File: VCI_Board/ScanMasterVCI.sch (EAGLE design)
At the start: 80 parts, among them IC1 XMEGA16A4A, IC2 CD4081B, IC3 SN74AHCT1G04, IC4 SN74AHCT1G04, IC6 TL331, IC7 74AHCT1G32DBV, IC8 SN74AHCT1G04, Q1 MMBT4403, Q2 MMBT4403LT1SMD, Q3 MMBT4403, Q4 MMBT3904, Q5 MMBT3904, Q6 MMBT4403, Q7 MMBT4403, Q8 MMBT4403, Q9 MMBT4403, U1 MAX17502FATB+, U3 MAX17502EATB+, U4 MAX13444EASA+

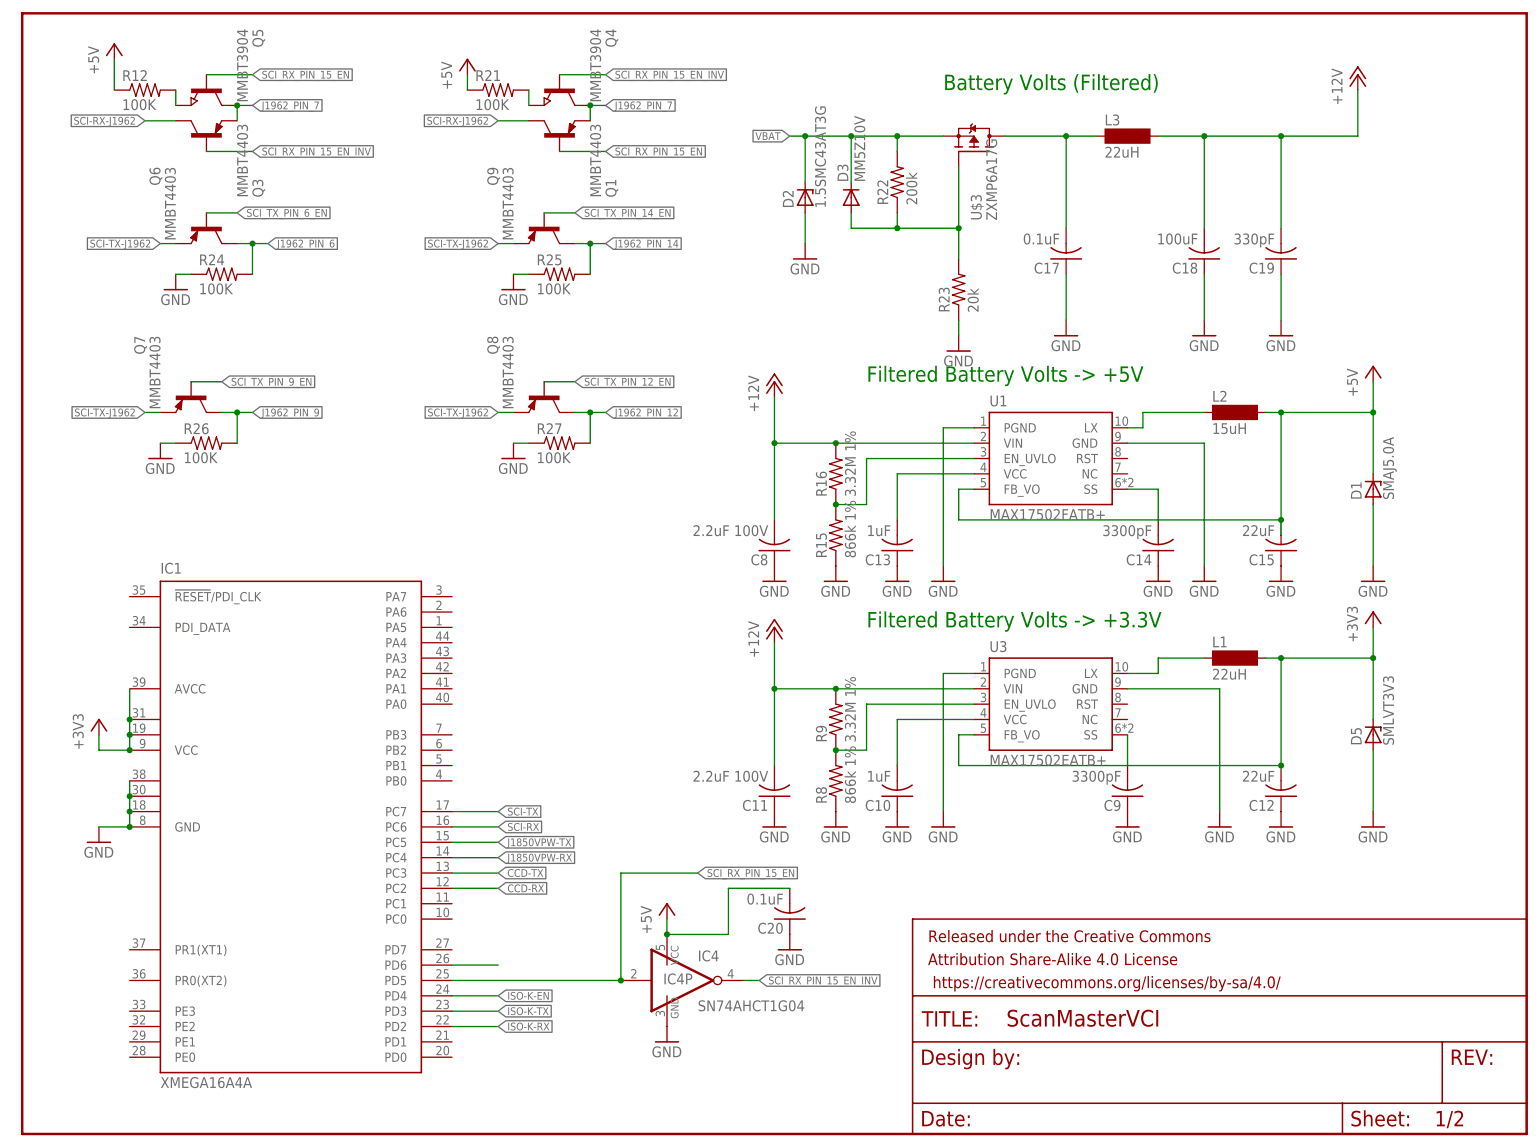
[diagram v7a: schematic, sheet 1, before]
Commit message: Added more sophisticated MUX for SCI. Moved around some pins to accomodate SPI programming. Added external headers for 4-pin RS-232, 6-pin ICSP, and 16-pin J1962.
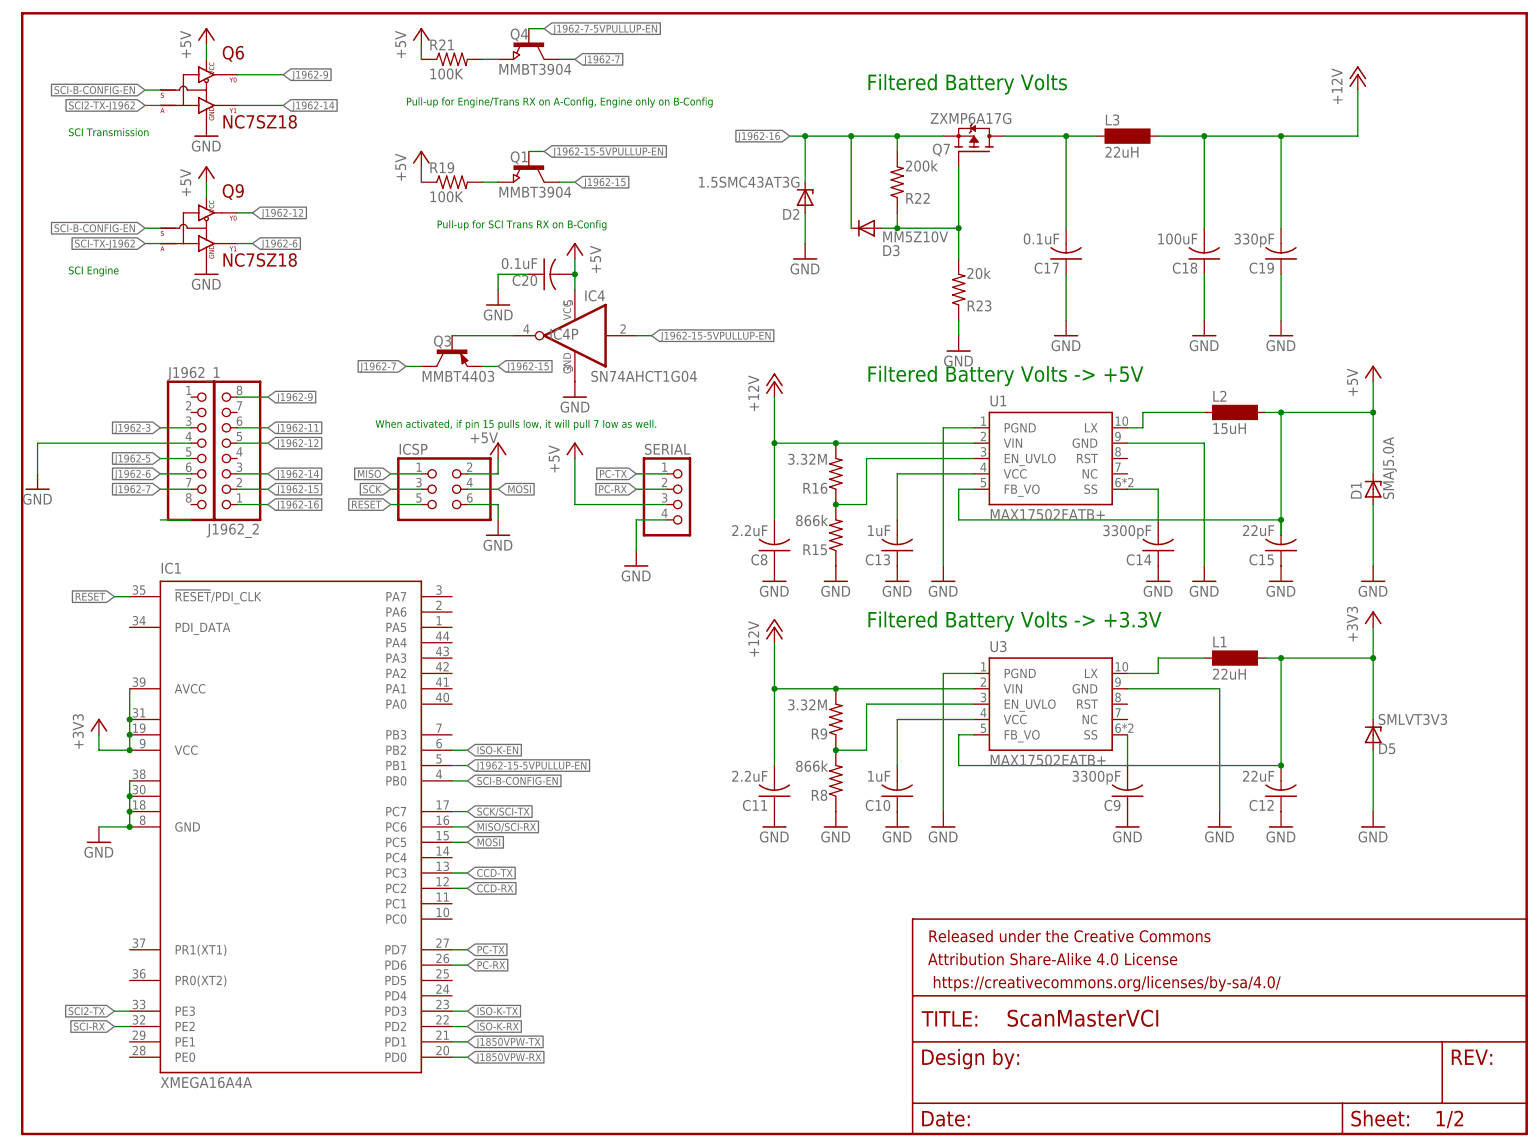
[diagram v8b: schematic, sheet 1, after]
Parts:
- removed IC3: SN74AHCT1G04, 74xx-little-us:74AHC1G04DBV
- removed Q5: MMBT3904, semicon-smd-ipc:NPN-TRANSISTOR_SOT23
- removed Q8: MMBT4403, transistor-pnp:MMBT4403LT1SMD
- removed R12, R18, R24, R25, R26, R27: 100K, adafruit:R-US_R0805W
- removed U$3: ZXMP6A17G, customics:ZXMP6A17G
- added ICSP: (no value), pinhead:PINHD-2X3
- added J1962_1, J1962_2: (no value), pinhead:PINHD-1X8
- added SERIAL: (no value), pinhead:PINHD-1X4
- C1, C16, C2, C3, C5, C6: value 0.1uF 16V -> 0.1uF
- C11, C8: value 2.2uF 100V -> 2.2uF
- C7: value 220pF 16V -> 220pF
- Q1: value MMBT4403 -> MMBT3904; device transistor-pnp:MMBT4403LT1SMD -> semicon-smd-ipc:NPN-TRANSISTOR_SOT23
- Q6, Q9: value MMBT4403 -> NC7SZ18; device transistor-pnp:MMBT4403LT1SMD -> customics:NC7SZ18
- Q7: value MMBT4403 -> ZXMP6A17G; device transistor-pnp:MMBT4403LT1SMD -> customics:ZXMP6A17G
- R15, R8: value 866k 1% -> 866k
- R16, R9: value 3.32M 1% -> 3.32M
- renumbered U$1 to D4, U$2 to U2
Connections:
- net J1962_PIN_2 renamed J1962-2
- removed net J1962_PIN_11: R1.1
- removed net J1962_PIN_12: Q8.C, R27.2
- removed net J1962_PIN_14: Q9.C, R25.2
- removed net J1962_PIN_3: R2.1
- removed net J1962_PIN_6: Q6.C, R24.2
- removed net J1962_PIN_7: C7.2, Q1.E, Q3.E, Q4.C, Q5.C, U2.LIN
- removed net J1962_PIN_9: Q7.C, R26.2
- removed net N$13: Q5.E, R12.2
- removed net N$22: IC1.PD6
- removed net SCI-RX-J1962: IC2C.I0, IC2C.I1, Q1.C, Q3.C
- removed net SCI_RX_PIN_15_EN: IC1.PD5, IC4A.I, Q1.B, Q5.B
- removed net SCI_RX_PIN_15_EN_INV: IC4A.O, Q3.B, Q4.B
- removed net SCI_TX_PIN_12_EN: Q8.B
- removed net SCI_TX_PIN_14_EN: Q9.B
- removed net SCI_TX_PIN_6_EN: Q6.B
- removed net SCI_TX_PIN_9_EN: Q7.B
- removed net VBAT: D2.C, D3.C, R22.2, U$3.S
- new net J1962-11: J1962_2.6, R1.1
- new net J1962-12: J1962_2.5, Q9.Y1
- new net J1962-14: J1962_2.3, Q6.Y0
- new net J1962-15: J1962_2.2, Q1.C, Q3.E
- new net J1962-15-5VPULLUP-EN: IC1.PB1, IC4A.I, Q1.B
- new net J1962-16: D2.C, D3.C, J1962_2.1, Q7.S, R22.2
- new net J1962-3: J1962_1.3, R2.1
- new net J1962-5: J1962_1.5
- new net J1962-6: J1962_1.6, Q9.Y0
- new net J1962-7: C7.2, IC2C.I0, IC2C.I1, J1962_1.7, Q3.C, Q4.C, U2.LIN
- new net J1962-7-5VPULLUP-EN: Q4.B
- new net J1962-9: J1962_2.8, Q6.Y1
- new net MISO: ICSP.1
- new net MISO/SCI-RX: IC1.PC6
- new net MOSI: IC1.PC5, ICSP.4
- new net N$10: IC4A.O, Q3.B
- new net N$25: Q1.E, R19.2
- new net PC-RX: IC1.PD6, SERIAL.2
- new net PC-TX: IC1.PD7, SERIAL.1
- new net RESET: IC1.!RESET!/PDI_CLK, ICSP.5
- new net SCI-B-CONFIG-EN: IC1.PB0, Q6.S, Q9.S
- new net SCI2-TX: IC1.PE3, IC2D.I0, IC2D.I1
- new net SCI2-TX-J1962: IC2D.O, Q6.A
- new net SCK: ICSP.3
- new net SCK/SCI-TX: IC1.PC7
- net +3V3: no longer R19.1
- net +5V: now also ICSP.2, Q6.VCC, Q9.VCC, R19.1, SERIAL.3; no longer IC3P.VCC, R12.1, R18.1
- net GND: now also ICSP.6, J1962_1.4, Q6.GND, Q9.GND, SERIAL.4; no longer IC3P.GND, R24.1, R25.1, R26.1, R27.1
- net ISO-K-EN: now also IC1.PB2; no longer IC1.PD4
- net J1850VPW-RX: now also IC1.PD0; no longer IC1.PC4
- net J1850VPW-TX: now also IC1.PD1; no longer IC1.PC5
- net N$18: now also Q7.D; no longer U$3.D
- net N$20: now also Q7.G; no longer U$3.G
- net SCI-RX: now also IC1.PE2; no longer IC1.PC6
- net SCI-TX: no longer IC1.PC7, R19.2
- net SCI-TX-J1962: now also Q9.A; no longer Q6.E, Q7.E, Q8.E, Q9.E, R18.2
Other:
- note added: "Filtered Battery Volts"
- note added: "Pull-up for Engine/Trans RX on A-Config, Engine only on B-Config"
- note added: "Pull-up for SCI Trans RX on B-Config"
- note added: "SCI Engine"
- note added: "SCI Transmission"
- note added: "When activated, if pin 15 pulls low, it will pull 7 low as well."
- note removed: "Battery Volts (Filtered)"
- moved on the sheet: C16, C20, C6, D3, IC2B, IC2C, IC4, IC4P, Q3, Q4, R20, R21
